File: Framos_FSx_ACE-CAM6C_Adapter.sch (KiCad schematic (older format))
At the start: 2 parts, among them J1 DF40C-60DP-0.4V_51_, J2 3-1734742-8

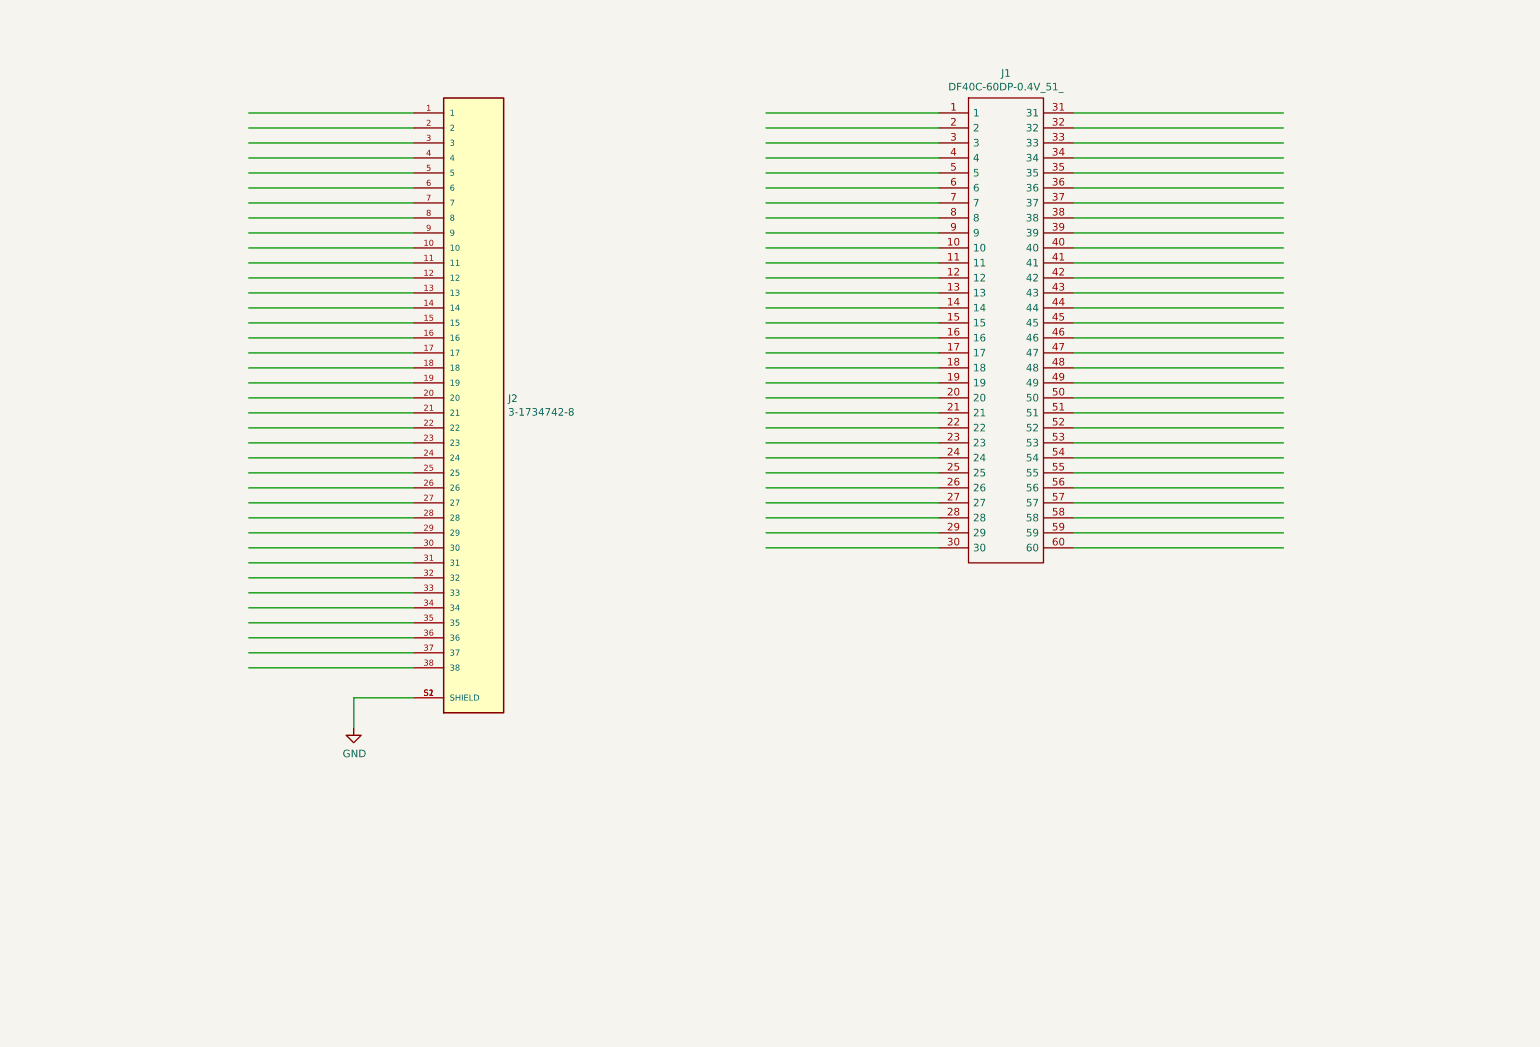
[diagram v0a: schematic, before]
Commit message: Add schematic drawing
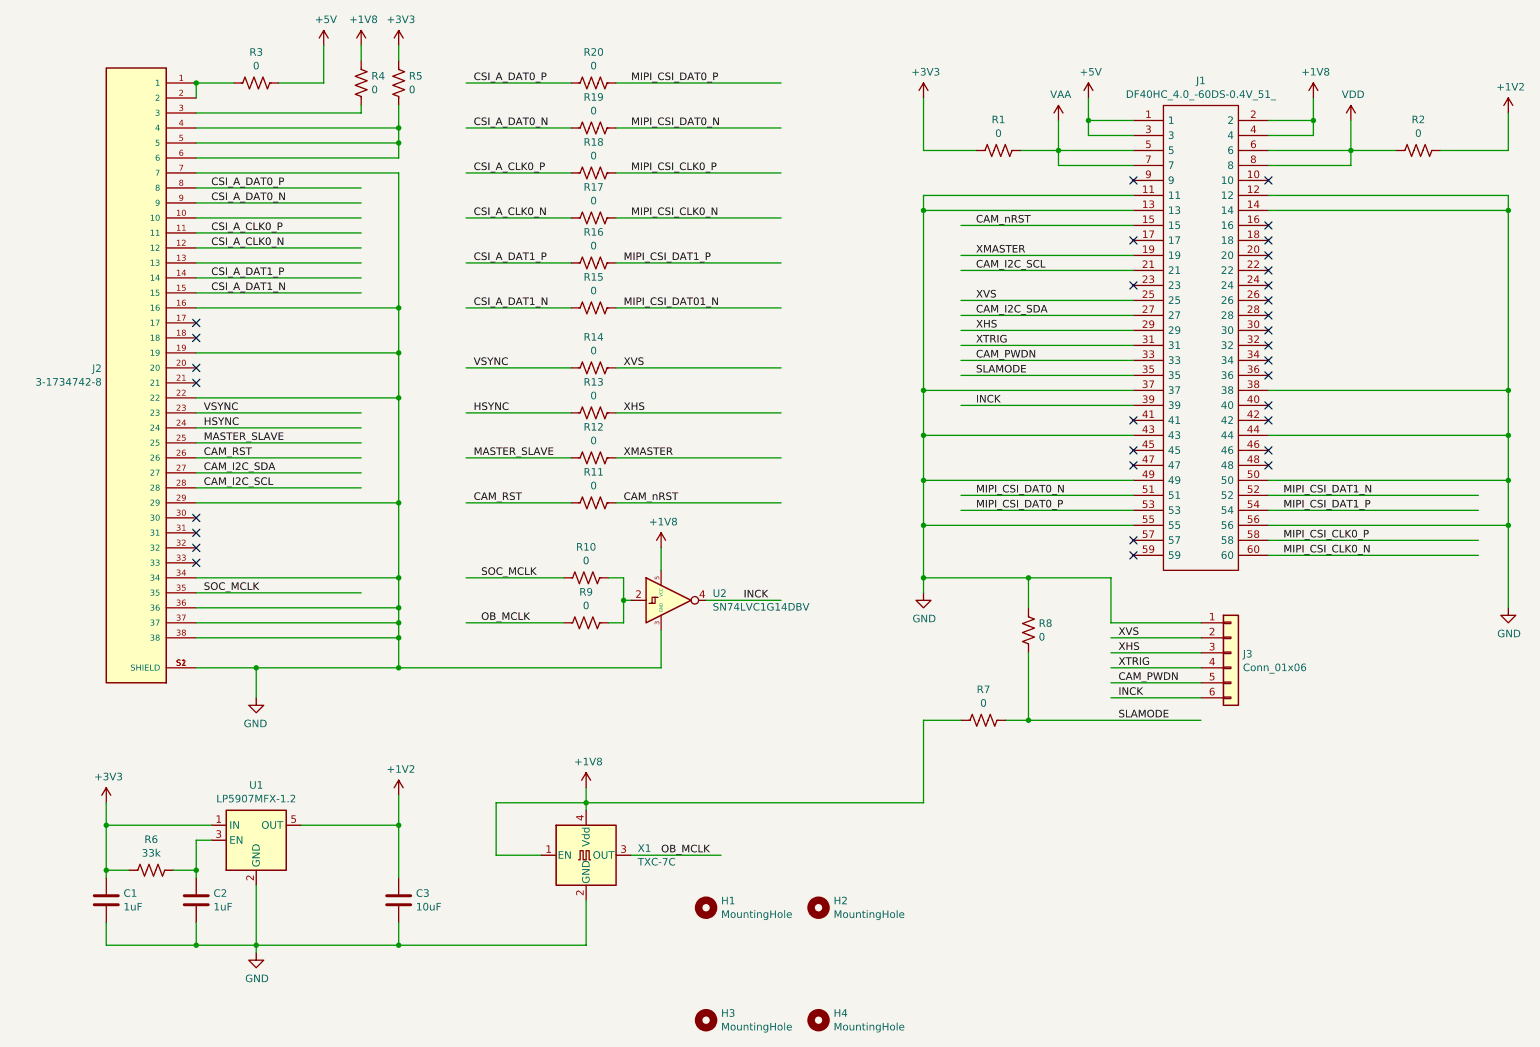
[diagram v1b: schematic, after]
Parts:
- removed J1: DF40C-60DP-0.4V_51_, DF40C-60DP-0.4V(51), symbol DF40C-60DP-0.4V_51_:DF40C-60DP-0.4V_51_
- added C1, C2: 1uF, symbol Device:C
- added C3: 10uF, symbol Device:C
- added H1, H2, H3, H4: MountingHole, symbol Mechanical:MountingHole
- added J1: DF40HC_4.0_-60DS-0.4V_51_, DF40HC4060DS04V51, symbol DF40HC_4.0_-60DS-0.4V_51_:DF40HC_4.0_-60DS-0.4V_51_
- added J3: Conn_01x06, symbol Connector_Generic:Conn_01x06
- added R1, R10, R11, R12, R13, R14, R15, R16, R17, R18, R19, R2, R20, R3, R4, R5, R7, R8, R9: 0, symbol Device:R_US
- added R6: 33k, symbol Device:R_US
- added U1: LP5907MFX-1.2, Package_TO_SOT_SMD:SOT-23-5, symbol Regulator_Linear:LP5907MFX-1.2
- added U2: SN74LVC1G14DBV, Package_TO_SOT_SMD:SOT-23-5, symbol 74xGxx:SN74LVC1G14DBV
- added X1: TXC-7C, Oscillator:Oscillator_SMD_TXC_7C-4Pin_5.0x3.2mm, symbol Oscillator:TXC-7C
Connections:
- net labels added: +1V2, +1V8, +3V3, +5V, CAM_I2C_SCL, CAM_I2C_SDA, CAM_PWDN, CAM_RST, CAM_nRST, CSI_A_CLK0_N, CSI_A_CLK0_P, CSI_A_DAT0_N, CSI_A_DAT0_P, CSI_A_DAT1_N, CSI_A_DAT1_P, HSYNC, INCK, MASTER_SLAVE, MIPI_CSI_CLK0_N, MIPI_CSI_CLK0_P, MIPI_CSI_DAT01_N, MIPI_CSI_DAT0_N, MIPI_CSI_DAT0_P, MIPI_CSI_DAT1_N, MIPI_CSI_DAT1_P, OB_MCLK, SLAMODE, SOC_MCLK, VAA, VDD, VSYNC, XHS, XMASTER, XTRIG, XVS
- wire segments 100 -> 188
- no-connect marks 0 -> 32
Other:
- moved on the sheet: J2

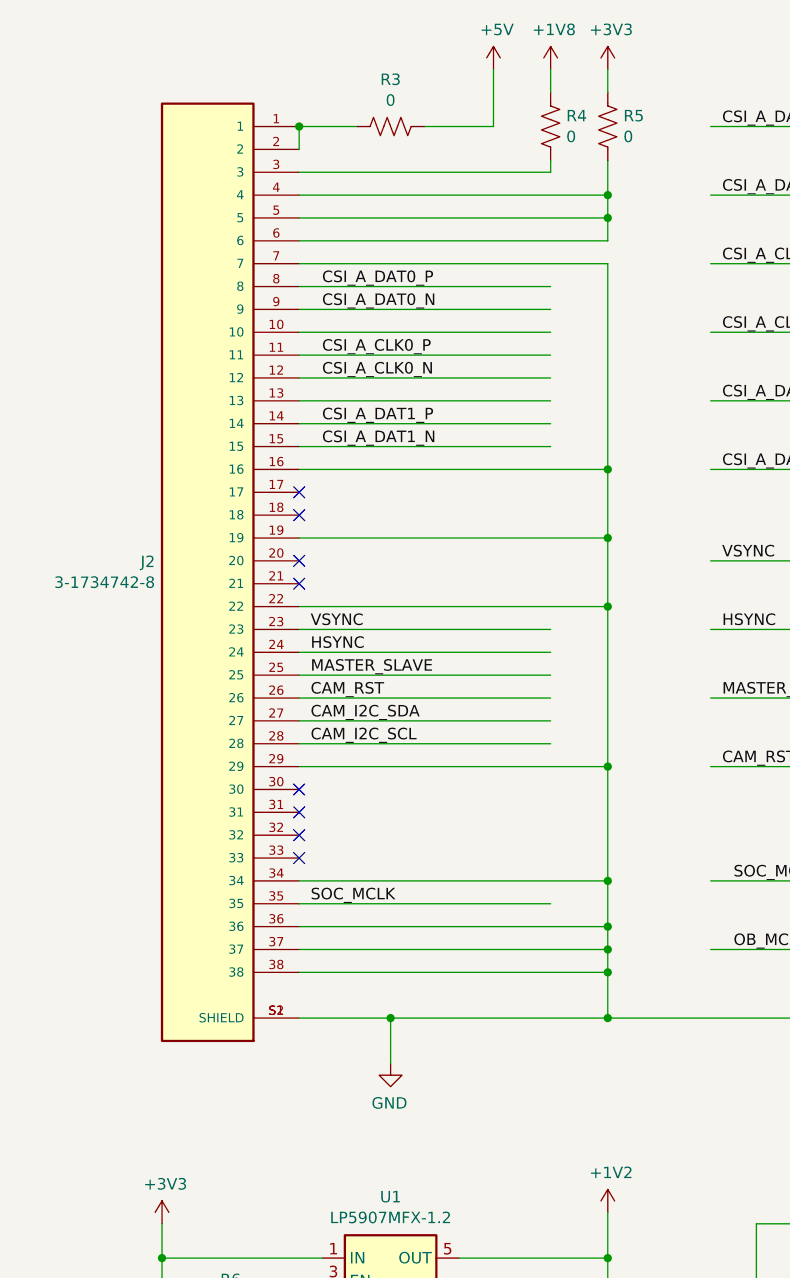
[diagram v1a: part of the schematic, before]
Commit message: Change component and associated libraries
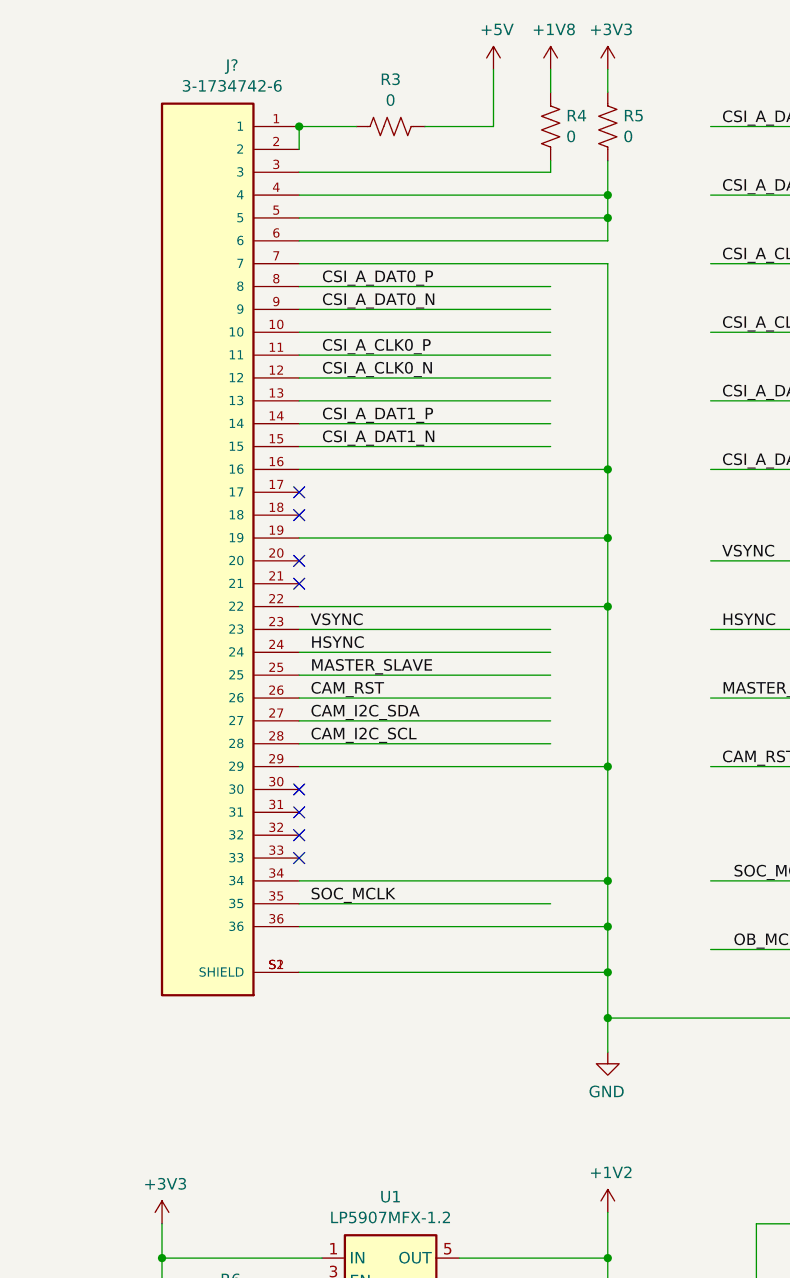
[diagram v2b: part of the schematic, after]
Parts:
- removed J2: 3-1734742-8, TE_3-1734742-8, symbol TE_3-1734742-8:3-1734742-8
- added J?: 3-1734742-6, TE_3-1734742-6, symbol TE_3-1734742-6:3-1734742-6
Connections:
- wire segments 188 -> 184
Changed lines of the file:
@@
 L power:GND #PWR?
 U 1 1 60BB8B26
-P 2400 5400
-F 0 "#PWR?" H 2400 5150 50  0001 C CNN
-F 1 "GND" H 2405 5227 50  0000 C CNN
-F 2 "" H 2400 5400 50  0001 C CNN
-F 3 "" H 2400 5400 50  0001 C CNN
-	1    2400 5400
+P 3350 5350
+F 0 "#PWR?" H 3350 5100 50  0001 C CNN
+F 1 "GND" H 3355 5177 50  0000 C CNN
+F 2 "" H 3350 5350 50  0001 C CNN
+F 3 "" H 3350 5350 50  0001 C CNN
+	1    3350 5350
 	-1   0    0    -1
 $EndComp
-Wire Wire Line
-	2000 5200 2400 5200
-Wire Wire Line
-	2400 5200 2400 5400
 $Comp
 L power:+5V #PWR?
@@
 Wire Wire Line
 	2000 1900 3350 1900
-Connection ~ 2400 5200
 Wire Wire Line
 	2000 4800 3350 4800
 Wire Wire Line
-	2000 4900 3350 4900
-Wire Wire Line
-	2000 5000 3350 5000
-Wire Wire Line
 	2000 4600 3350 4600
 Wire Wire Line
@@
 Wire Wire Line
 	2000 2800 3350 2800
-$Comp
-L TE_3-1734742-8:3-1734742-8 J2
-U 1 1 60AB4834
-P 1600 3200
-F 0 "J2" H 1830 3196 50  0000 L CNN
-F 1 "3-1734742-8" H 1830 3105 50  0000 L CNN
-F 2 "TE_3-1734742-8" H 1600 3200 50  0001 L BNN
-F 3 "" H 1600 3200 50  0001 L BNN
-F 4 "P" H 1600 3200 50  0001 L BNN "PARTREV"
-F 5 "5.30mm" H 1600 3200 50  0001 L BNN "MAXIMUM_PACKAGE_HEIGHT"
-F 6 "TE Connectivity" H 1600 3200 50  0001 L BNN "MANUFACTURER"
-F 7 "Manufacturer Recommendations" H 1600 3200 50  0001 L BNN "STANDARD"
-	1    1600 3200
-	-1   0    0    -1
-$EndComp
 $Comp
 L Device:R_US R1
@@
 	3350 4600 3350 4800
 Connection ~ 3350 4800
-Wire Wire Line
-	3350 4800 3350 4900
-Connection ~ 3350 4900
-Wire Wire Line
-	3350 4900 3350 5000
-Connection ~ 3350 5000
-Wire Wire Line
-	3350 5000 3350 5200
-Wire Wire Line
-	3350 5200 2400 5200
 $Comp
 L Mechanical:MountingHole H1
@@
 Wire Wire Line
 	2000 1300 2250 1300
-Connection ~ 2000 1300
 Wire Wire Line
 	9150 2150 10750 2150
@@
 Wire Wire Line
 	3350 5200 5100 5200
-Connection ~ 3350 5200
 Wire Wire Line
 	3800 4600 4450 4600
@@
 	0    1    1    0
 $EndComp
+Wire Wire Line
+	3350 5000 3350 5200
+Connection ~ 3350 5000
+Wire Wire Line
+	2000 5000 3350 5000
+$Comp
+L TE_3-1734742-6:3-1734742-6 J?
+U 1 1 61609C92
+P 1600 3100
+F 0 "J?" H 1493 5167 50  0000 C CNN
+F 1 "3-1734742-6" H 1493 5076 50  0000 C CNN
+F 2 "TE_3-1734742-6" H 1600 3100 50  0001 L BNN
+F 3 "" H 1600 3100 50  0001 L BNN
+F 4 "5.30mm" H 1600 3100 50  0001 L BNN "MAXIMUM_PACKAGE_HEIGHT"
+F 5 "Manufacturer Recommendations" H 1600 3100 50  0001 L BNN "STANDARD"
+F 6 "P" H 1600 3100 50  0001 L BNN "PARTREV"
+F 7 "TE Connectivity" H 1600 3100 50  0001 L BNN "MANUFACTURER"
+	1    1600 3100
+	-1   0    0    -1
+$EndComp
+Connection ~ 2000 1300
+Wire Wire Line
+	3350 4800 3350 5000
+Wire Wire Line
+	3350 5200 3350 5350
+Connection ~ 3350 5200
 $EndSCHEMATC

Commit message: Change schemtic component
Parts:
- gave numbers to parts that had none: 1
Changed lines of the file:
@@
 	2000 5000 3350 5000
 $Comp
-L TE_3-1734742-6:3-1734742-6 J?
+L TE_3-1734742-6:3-1734742-6 J2
 U 1 1 61609C92
 P 1600 3100
-F 0 "J?" H 1493 5167 50  0000 C CNN
+F 0 "J2" H 1493 5167 50  0000 C CNN
 F 1 "3-1734742-6" H 1493 5076 50  0000 C CNN
 F 2 "TE_3-1734742-6" H 1600 3100 50  0001 L BNN

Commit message: Assign footprints and genrate netlist
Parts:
- C1, C2, C3: footprint (none) -> Capacitor_SMD:C_0603_1608Metric_Pad1.08x0.95mm_HandSolder
- H1, H2, H3, H4: footprint (none) -> MountingHole:MountingHole_2.2mm_M2
- J1: footprint DF40HC4060DS04V51 -> footprints:DF40HC4060DS04V51
- J2: footprint TE_3-1734742-6 -> footprints:TE_3-1734742-6
- J3: footprint (none) -> Connector_PinHeader_2.54mm:PinHeader_1x06_P2.54mm_Vertical
- R1, R10, R11, R12, R13, R14, R15, R16, R17, R18, R19, R2, R20, R3, R4, R5, R6, R7, R8, R9: footprint (none) -> Resistor_SMD:R_0805_2012Metric_Pad1.20x1.40mm_HandSolder
